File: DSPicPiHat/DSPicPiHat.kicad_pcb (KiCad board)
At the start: 2 copper layers, 65 x 66.5 mm, 92 parts, among them J1 Conn_01x09_Female, J2 Conn_01x04_Female, J4 Conn_PIC_ICSP_ICD, J5 USB_C_Receptacle_USB2.0, J6 PowerInput, J8 RasPiHeaders, SW1 POWER_Select, SW2 SW_DIP_x08, U1 DSPIC33CH512MP508T-I_PT, U10 DF5A6.2CJE_LM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

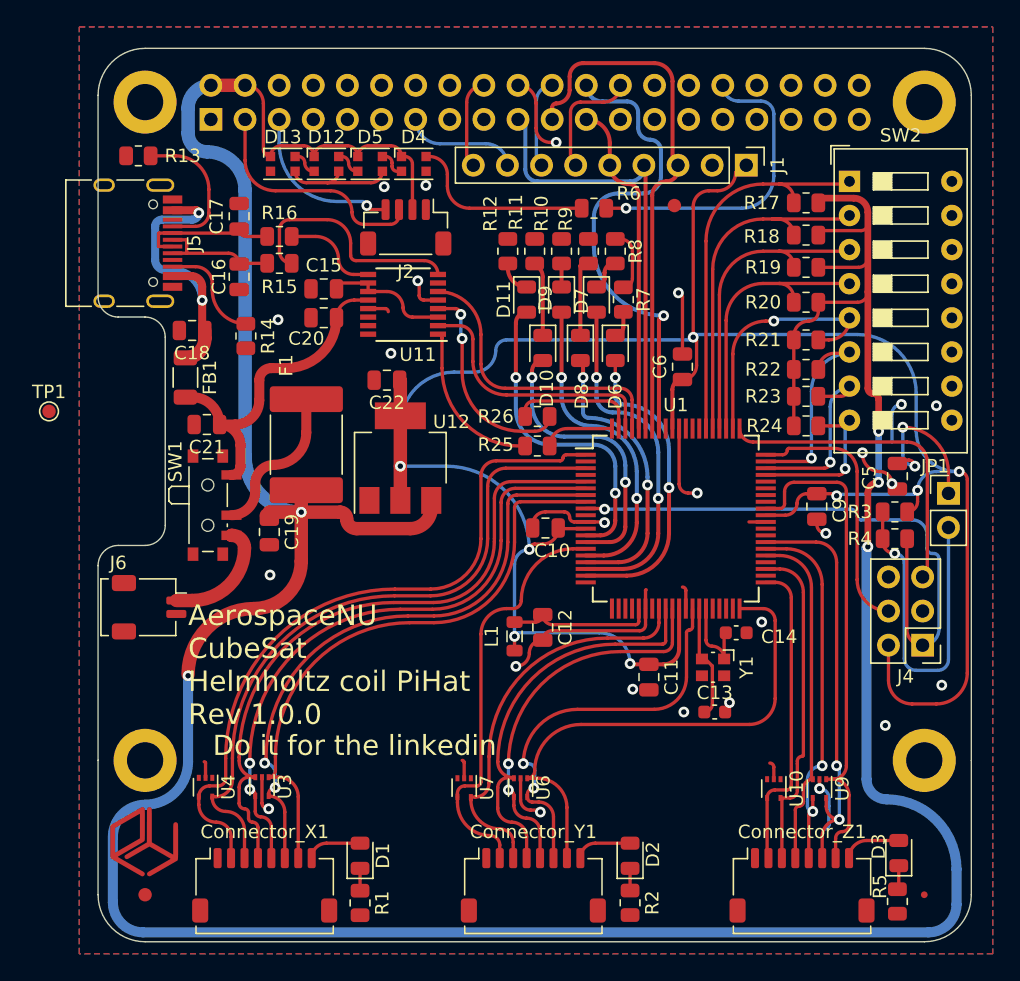
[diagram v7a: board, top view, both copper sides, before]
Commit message: made a few traces slightly thicker
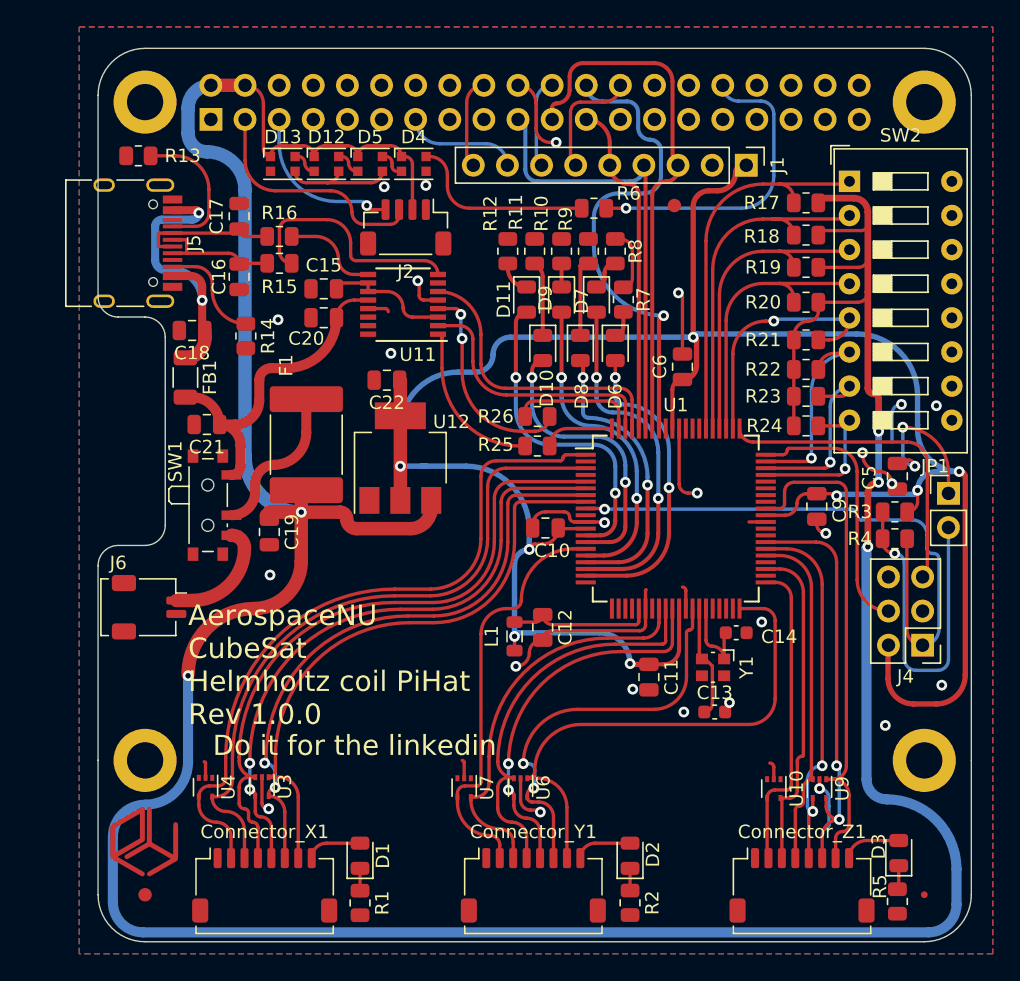
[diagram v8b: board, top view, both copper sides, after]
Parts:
- removed TP1: TestPoint, TestPoint:TestPoint_Pad_D1.0mm
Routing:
- net VDD: track 174.8 -> 176.2 mm
